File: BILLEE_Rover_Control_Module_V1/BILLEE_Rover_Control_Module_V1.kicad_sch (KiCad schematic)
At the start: 0 parts

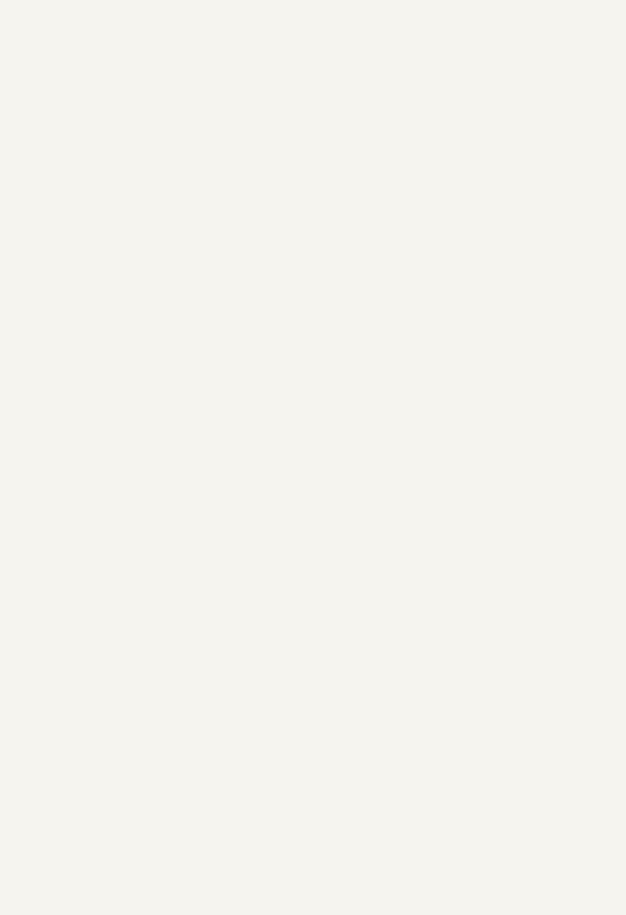
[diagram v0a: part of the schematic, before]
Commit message: temporary push
Added the gate driver and its mosfet started the set up, but yet to confirm its connections and values. will do when i get home
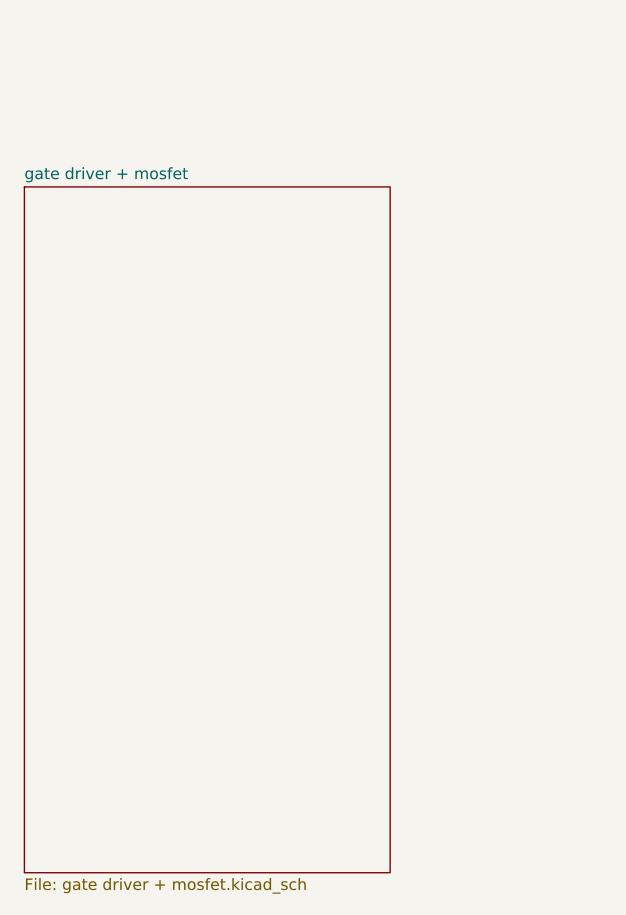
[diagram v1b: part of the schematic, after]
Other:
- added sheet gate driver + mosfet (gate driver + mosfet.kicad_sch)
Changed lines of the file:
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@@
+	)
+	(sheet
+		(at 524.51 135.89)
+		(size 40.64 76.2)
+		(exclude_from_sim no)
+		(in_bom yes)
+		(on_board yes)
+		(dnp no)
+		(fields_autoplaced yes)
+		(stroke
+			(width 0.1524)
+			(type solid)
+		)
+		(fill
+			(color 0 0 0 0)
+		)
+		(property "Sheetname" "gate driver + mosfet"
+			(at 524.51 135.1784 0)
+			(show_name no)
+			(do_not_autoplace no)
+			(effects
+				(font
+					(size 1.27 1.27)
+				)
+				(justify left bottom)
+			)
+		)
+		(property "Sheetfile" "gate driver + mosfet.kicad_sch"
+			(at 524.51 212.6746 0)
+			(show_name no)
+			(do_not_autoplace no)
+			(effects
+				(font
+					(size 1.27 1.27)
+				)
+				(justify left top)
+			)
+		)
+		(instances
+			(project "BILLEE_Rover_Control_Module_V1"
+				(path "/e701dc98-f022-461d-84b5-6b2dd8d89d58"
+					(page "5")
+				)
+			)
+		)
 	)
 	(sheet

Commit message: WIP Checkpoint
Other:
- sheet E-STOP Circuit renamed E-STOP / Drivetrain / Arm / Science Breakout
- sheet MCU RP2350A renamed RP2350A
- sheet Power renamed Logic Power

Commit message: Goodies
Updated all schematics
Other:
- sheet E-STOP / Drivetrain / Arm / Science Breakout renamed Subsystem Power Control
- sheet Logic Power renamed Logic Subsystem
- removed sheet gate driver + mosfet
- note added: "+14.4V XT-60 ARM"
- note added: "+14.4V XT-60 Drivetrain"
- note added: "+14.4V XT-60 Science"
- note added: "+24V PoE"
- note added: "2x14.4/1x22.2"
- note added: "5x Arducam"
- note added: "API"
- note added: "Adapter"
- note added: "BILLEE ROVER"
- note added: "Batteries"
- note added: "CAN Drivetrain"
- note added: "CAT5E"
- note added: "COMPUTA..DO.."
- note added: "COTS +24V POE"
- note added: "COTS Eth SW"
- note added: "Coax"
- note added: "Control"
- note added: "DSI"
- note added: "ESTOP Sense"
- note added: "F` GDS Serial USB-C"
- note added: "Functional Block Diagram"
- note added: "GPIO/SPI/UART/I2C Breakout"
- note added: "Ground Station"
- note added: "I2C0/1 Temp/Power Sense"
- note added: "Intel Realsense"
- note added: "Jetson"
- note added: "Middleware"
- note added: "OR"
- note added: "OoooOO radio waves"
- note added: "PoE Adapter"
- note added: "SERIAL/CAN Arm"
- note added: "Subsystem Power Control"
- note added: "USB Serial. Full Duplex. 8-1N 115200 BAUD. USB Type B"
- note added: "USB-C"
- note added: "Ubiquiti Antenna"
- note added: "Ubiquiti Prism"
- note added: "XT-60"
- note added: "Zed 2"
- note added: "ubuntu_arm64"
- company: (none) -> Bronco STAR
- title: (none) -> BILLEE_RCM
